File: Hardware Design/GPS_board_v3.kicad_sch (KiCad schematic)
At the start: 16 parts, among them IC2 SN65HVD231QDR, IC3 PIC18F26Q84-I_SS, U5 MAX-M8W

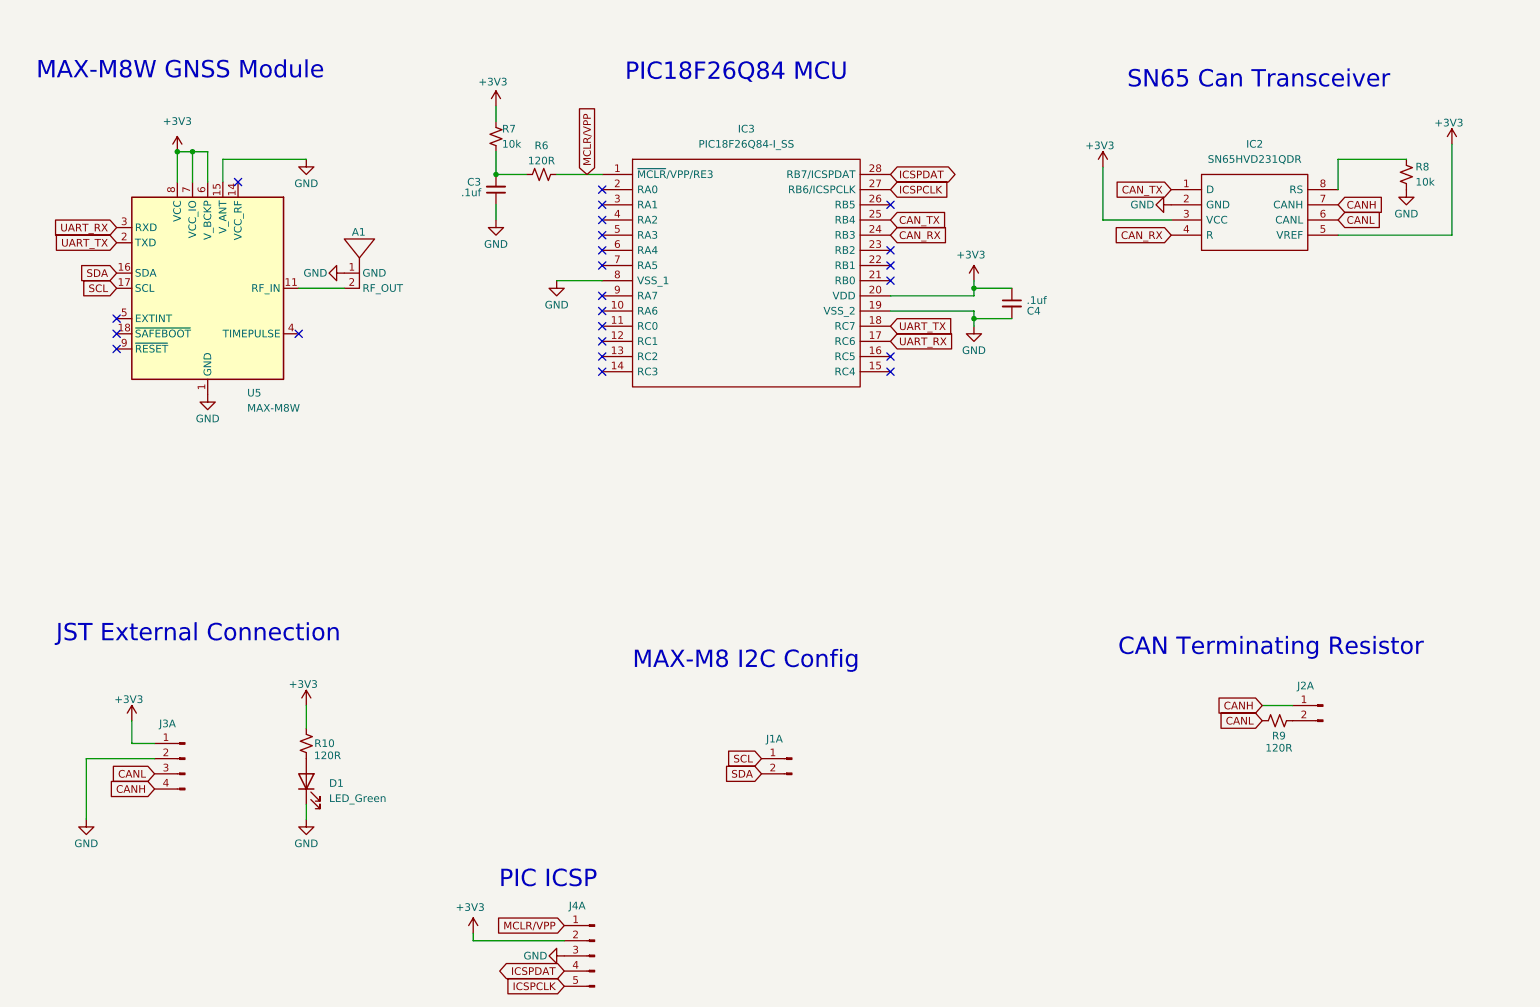
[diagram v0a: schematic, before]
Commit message: redesigned board for STM32
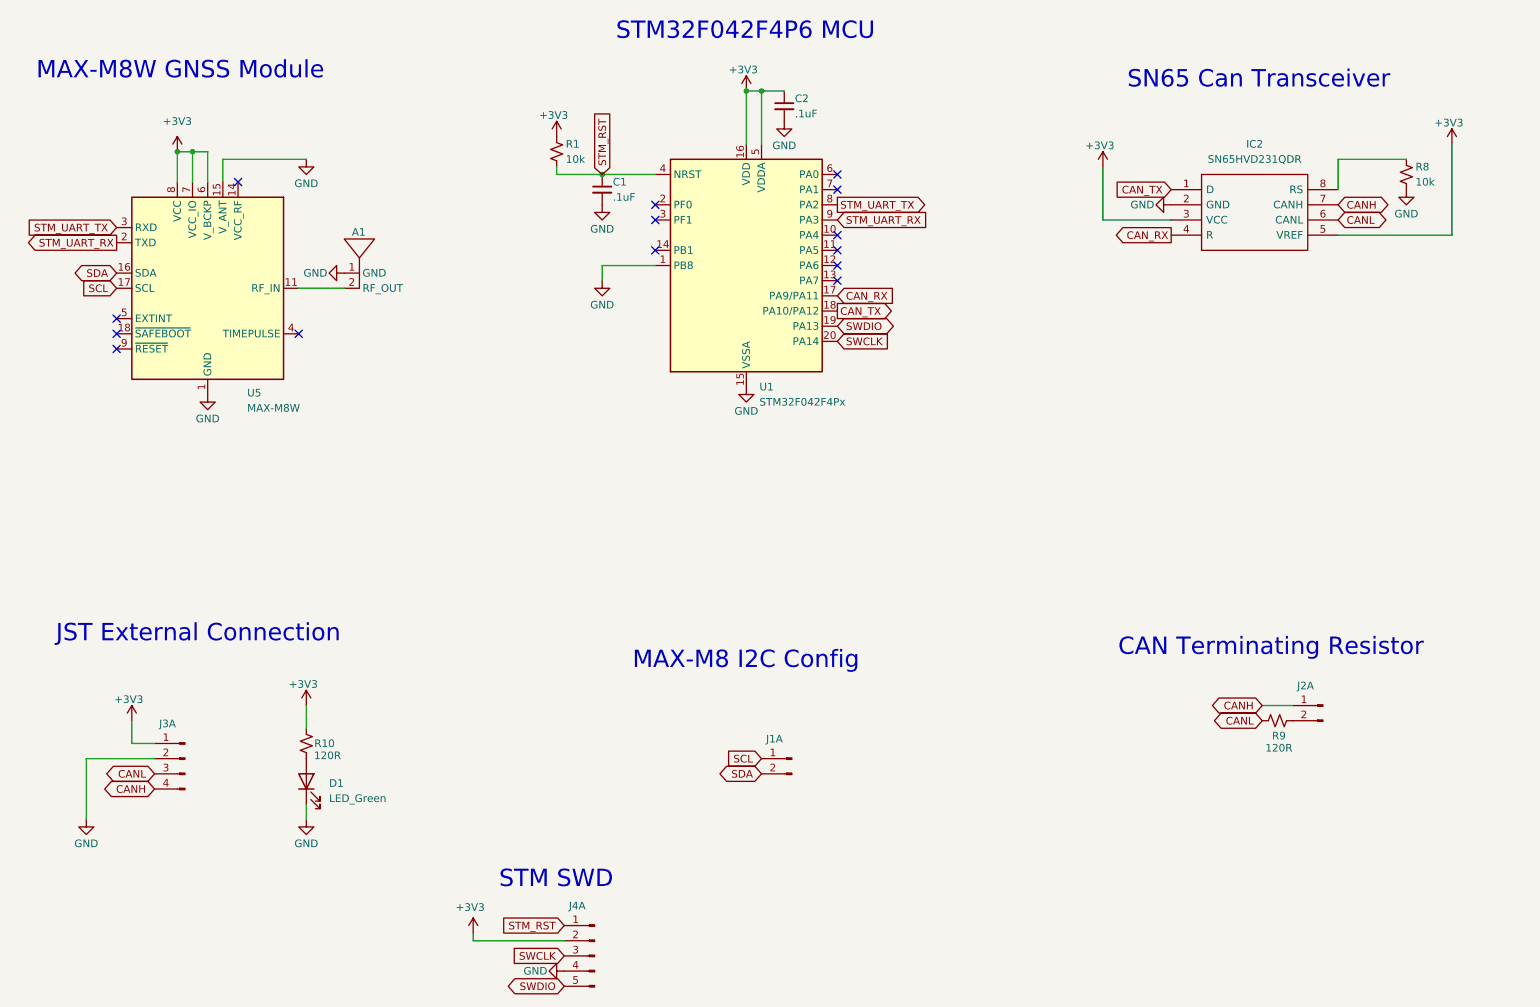
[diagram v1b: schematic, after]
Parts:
- removed C3, C4: .1uf, Capacitor_SMD:C_0805_2012Metric_Pad1.18x1.45mm_HandSolder, symbol Device:C_Small
- removed IC3: PIC18F26Q84-I_SS, Package_SO:SOP65P780X200-28N, symbol MCU_Microchip_PIC18:PIC18F26Q84-I_SS
- removed R6: 120R, Resistor_SMD:R_0805_2012Metric_Pad1.20x1.40mm_HandSolder, symbol Device:R_Small_US
- removed R7: 10k, Resistor_SMD:R_0805_2012Metric_Pad1.20x1.40mm_HandSolder, symbol Device:R_Small_US
- added C1, C2: .1uF, Capacitor_SMD:C_0805_2012Metric, symbol Device:C_Small
- added R1: 10k, Resistor_SMD:R_0805_2012Metric_Pad1.20x1.40mm_HandSolder, symbol Device:R_Small_US
- added U1: STM32F042F4Px, Package_SO:TSSOP-20_4.4x6.5mm_P0.65mm, symbol MCU_ST_STM32F0:STM32F042F4Px
- J3: footprint Connector_JST:JST_SH_SM04B-SRSS-TB_1x04-1MP_P1.00mm_Horizontal -> Connector_PinHeader_2.54mm:PinHeader_1x04_P2.54mm_Vertical
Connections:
- net ICSPDAT is gone; now on net GND: J4.4 (Pin_4)
- net +3V3: now also C2.1, R1.1, U1.16 (VDD), U1.5 (VDDA)
- net CAN_RX: now also U1.17 (PA9/PA11)
- net CAN_TX: now also U1.18 (PA10/PA12)
- net GND: now also C1.2, C2.2, U1.1 (PB8), U1.15 (VSSA); no longer J4.3 (Pin_3)
- net ICSPCLK renamed SWDIO
- net SWDIO: now also U1.19 (PA13)
- net MCLR/VPP renamed STM_RST
- net STM_RST: now also C1.1, R1.2, U1.4 (NRST)
- net UART_RX renamed STM_UART_TX
- net STM_UART_TX: now also U1.8 (PA2)
- net UART_TX renamed STM_UART_RX
- net STM_UART_RX: now also U1.9 (PA3)
- new net SWCLK: J4.3 (Pin_3), U1.20 (PA14)
- no-connect marks 23 -> 14
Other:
- note added: "STM SWD"
- note added: "STM32F042F4P6 MCU"
- note removed: "PIC ICSP"
- note removed: "PIC18F26Q84 MCU"
- title: PIC18 GPS Board -> STM32 GPS Board
